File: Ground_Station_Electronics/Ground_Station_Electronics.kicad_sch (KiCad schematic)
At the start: 4 parts

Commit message: worked on rs485
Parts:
- removed J?: (no value), symbol Connector:RJ45_Shielded
- removed R?: R_Small, symbol Device:R_Small
- added C? (x2): 33u, symbol Device:C_Polarized_Small
- added C?: (no value), symbol Device:C_Small
- added C?: (no value), symbol Device:C_Polarized_Small
- added J?: (no value), symbol GS_Library:RJ45_Shielded_Labelled
- added R?: 120, Resistor_SMD:R_0603_1608Metric, symbol Device:R_Small
- U?: value (none) -> MAX3488E; footprint (none) -> Package_SO:SOIC-8_3.9x4.9mm_P1.27mm
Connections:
- net at R?.1: now also U?.5 (Y), J?.6 (ORG)
- net at R?.2: now also U?.6 (Z), J?.3 (~{ORG})
- net +3V3: now reaches U?.1 (VCC)
- net +3V3: now also C?.2
- net GND: now reaches U?.4 (GND)
- net GND: now also C?.1, C?.2, C?.2, C?.2, J?.7 (~{BRN}), J?.8 (BRN), J?.SH
- net at U?.7 (B): now also J?.1 (~{GRN}), R?.2
- net at U?.8 (A): now also J?.2 (GRN), R?.1
- new net +12V: C?.1, C?.1, C?.1, J?.4 (BLU), J?.5 (~{BLU})
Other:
- moved on the sheet: R?, U?

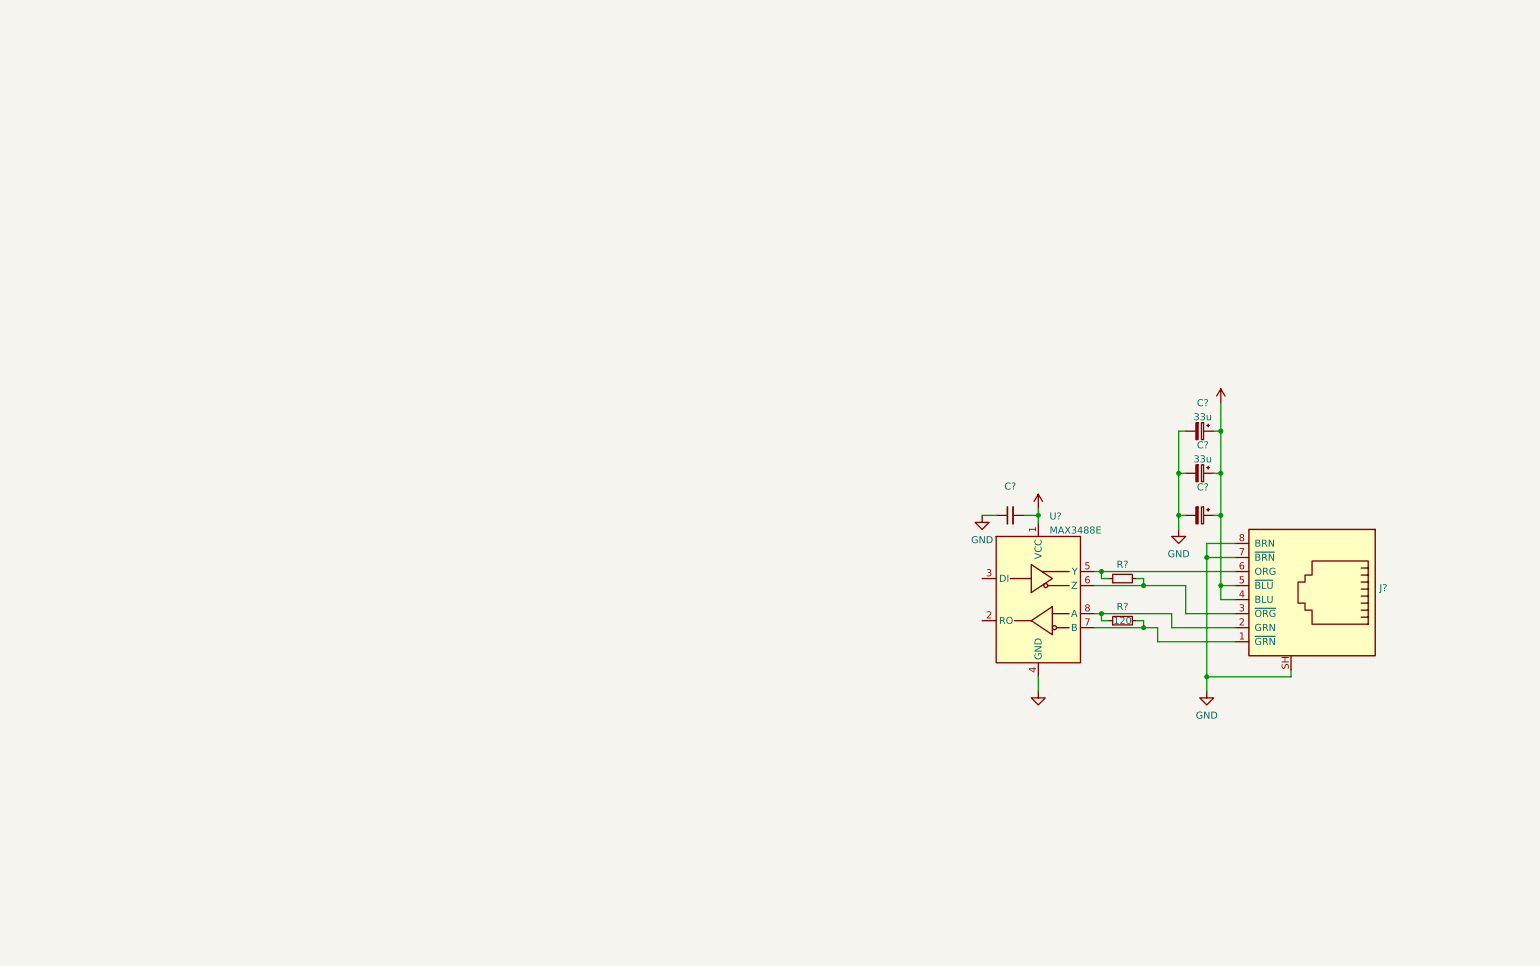
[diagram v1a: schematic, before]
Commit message: Take 2 Electric Boogaloo
Migrated to KiCad 6.0. Re-added the schematic stuff from last time in the new version, hopefully with working libraries
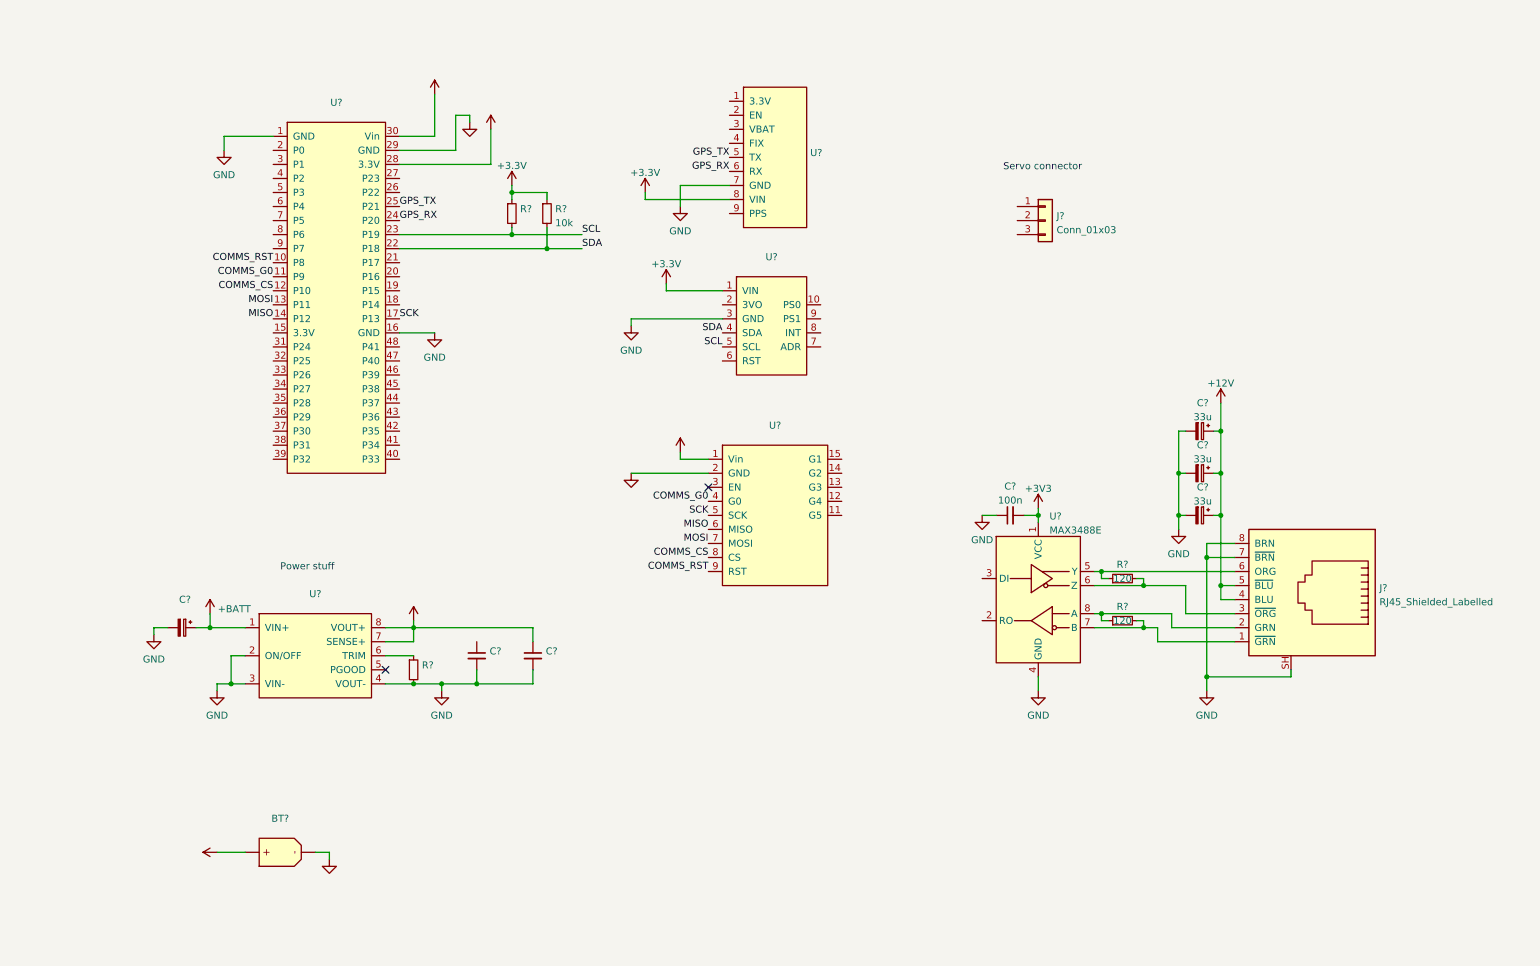
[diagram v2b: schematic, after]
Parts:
- added BT?: (no value), symbol ASTRA_Library:XT60_Battery_Connector
- added C? (x2): (no value), symbol Device:C_Small
- added C?: (no value), symbol Device:C_Polarized_Small
- added J?: Conn_01x03, symbol Connector_Generic:Conn_01x03
- added R?: 10k, symbol Device:R_Small
- added R? (x2): (no value), symbol Device:R_Small
- added U?: (no value), symbol MainElectronicsLib:BNO055_Adafruit_Breakout
- added U?: (no value), symbol ASTRA_Library:Teensy_4.1
- added U?: (no value), symbol ASTRA_Library:Adafruit_GPS_V3
- added U?: (no value), symbol MainElectronicsLib:RFM95W_Adafruit_Breakout
- added U?: (no value), symbol ASTRA_Library:TDK_I3A4W008A033V
- C?: value (none) -> 100n; footprint (none) -> Capacitor_SMD:C_0603_1608Metric
- C?: value (none) -> 33u
- J?: value (none) -> RJ45_Shielded_Labelled
- R?: value (none) -> 120; footprint (none) -> Resistor_SMD:R_0603_1608Metric
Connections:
- net +3V3: now also R?.1, R?.1, U?.1 (VIN), U?.1 (Vin), U?.28 (3.3V), U?.8 (VIN)
- net GND: now also BT?.1 (Neg), C?.2, C?.2, C?.2, R?.2, U?.1 (GND), U?.16 (GND), U?.2 (GND), U?.2 (ON/OFF), U?.29 (GND), U?.3 (GND), U?.3 (VIN-), U?.4 (VOUT-), U?.7 (GND)
- new net: R?.1, U?.6 (TRIM)
- new net +5V: C?.1, U?.30 (Vin), U?.7 (SENSE+), U?.8 (VOUT+)
- new net +BATT: BT?.2 (Pos), C?.1, U?.1 (VIN+)
- new net COMMS_CS: U?.12 (P10), U?.8 (CS)
- new net COMMS_G0: U?.11 (P9), U?.4 (G0)
- new net COMMS_RST: U?.10 (P8), U?.9 (RST)
- new net GPS_RX: U?.24 (P20), U?.6 (RX)
- new net GPS_TX: U?.25 (P21), U?.5 (TX)
- new net MISO: U?.14 (P12), U?.6 (MISO)
- new net MOSI: U?.13 (P11), U?.7 (MOSI)
- new net SCK: U?.17 (P13), U?.5 (SCK)
- new net SCL: R?.2, U?.23 (P19), U?.5 (SCL)
- new net SDA: R?.2, U?.22 (P18), U?.4 (SDA)
- no-connect marks 0 -> 2
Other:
- note added: "Power stuff"
- note added: "Servo connector"

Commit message: Working on schematic
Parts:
- removed C? (x2): (no value), symbol Device:C_Small
- removed C?: (no value), symbol Device:C_Polarized_Small
- removed J?: Conn_01x03, symbol Connector_Generic:Conn_01x03
- removed R?: (no value), symbol Device:R_Small
- removed U?: (no value), symbol ASTRA_Library:TDK_I3A4W008A033V
- added C1, C2: (no value), symbol Device:C_Polarized_Small_US
- added C3: 100u, symbol Device:C_Polarized_Small_US
- added C8: 1m, symbol Device:C_Polarized_Small_US
- added C9: 100n, Capacitor_SMD:C_0603_1608Metric, symbol Device:C_Small
- added D1: (no value), symbol Device:D_Schottky
- added D2: (no value), symbol Device:LED_Small
- added D3, D4: G, LED_SMD:LED_0603_1608Metric_Pad1.05x0.95mm_HandSolder, symbol Device:LED_Small
- added J2: (no value), symbol Connector_Generic:Conn_01x03
- added L1: (no value), symbol Device:L
- added M1: (no value), symbol GS_Library:Motor_Servo
- added M2: Motor_Servo, symbol GS_Library:Motor_Servo
- added R1, R2, R4: (no value), symbol Device:R_Small
- added U1: (no value), symbol Regulator_Switching:LM2576HVS-5
- added U7: (no value), symbol ASTRA_Library:SN74AHCT125D
- C5, C6: renamed from C?; symbol Device:C_Polarized_Small -> Device:C_Polarized_Small_US
- C7: renamed from C?; value 33u -> (none); symbol Device:C_Polarized_Small -> Device:C_Polarized_Small_US
- R3: renamed from R?; value (none) -> 10k
- U2: renamed from U?; value (none) -> Teensy_4.1
- U3: renamed from U?; value (none) -> Adafruit_GPS_V3
- U4: renamed from U?; value (none) -> BNO055_Adafruit_Breakout
- U5: renamed from U?; value (none) -> RFM95W_Adafruit_Breakout
- gave numbers to parts that had none: 7
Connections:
- net +BATT is gone; now on net +24V: BT1.2 (Pos)
- net +3V3: now also D2.2 (A)
- net +5V: now also C2.1, C3.1, C8.1, C9.2, D3.2 (A), J2.1 (Pin_1), L1.2, M1.2 (+), M2.2 (+), U1.4 (FB), U7.14 (VCC)
- net GND: now also C1.2, C2.2, C3.2, C8.2, C9.1, D1.2 (A), J2.2 (Pin_2), M1.3 (-), M2.3 (-), R1.2, R2.2, R4.2, U1.3 (GND), U1.5 (~{ON}/OFF), U7.1 (1~{OE}), U7.10 (3~{OE}), U7.11 (4Y), U7.12 (4A), U7.13 (4~{OE}), U7.4 (2~{OE}), U7.5 (2A), U7.6 (2Y), U7.7 (GND), U7.8 (3Y), U7.9 (3A)
- net COMP_RX: now reaches U6.2 (RO)
- net COMP_RX: now also U2.3 (P1)
- net COMP_TX: now reaches U6.3 (DI)
- net COMP_TX: now also U2.2 (P0)
- net SRV1_PWM: now reaches U2.4 (P2)
- net SRV1_PWM: now also M1.1 (PWM)
- net SRV2_PWM: now reaches U2.5 (P3)
- net SRV2_PWM: now also M2.1 (PWM)
- net +12V renamed +24V
- net +24V: now also C1.1, D4.2 (A), U1.1 (VIN)
- new net: D3.1 (K), R2.1
- new net: J2.3 (Pin_3), U7.3 (1Y)
- new net: D4.1 (K), R4.1
- new net: D1.1 (K), L1.1, U1.2 (OUT)
- new net: D2.1 (K), R1.1
- no-connect marks 2 -> 1
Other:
- note removed: "Servo connector"

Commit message: worked on schematic and footprints
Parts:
- C1: Digikey Part Num (none) -> 50PEV100M10X10.5CT-ND
- C2: Digikey Part Num (none) -> P16300-ND
- C3: value 100u -> (none); Digikey Part Num (none) -> 50PEV100M10X10.5CT-ND
- C4, C9: value 100n -> (none); footprint Capacitor_SMD:C_0603_1608Metric -> (none)
- C5, C6: value 33u -> (none); Digikey Part Num (none) -> 493-4402-1-ND
- C7: Digikey Part Num (none) -> 493-4402-1-ND
- C8: value 1m -> (none); Digikey Part Num (none) -> P16300-ND
- D1: Digikey Part Num (none) -> B560C-FDICT-ND
- D3, D4: value G -> (none); footprint LED_SMD:LED_0603_1608Metric_Pad1.05x0.95mm_HandSolder -> (none)
- J1: value RJ45_Shielded_Labelled -> (none); Digikey Part Num (none) -> AE10387-ND
- L1: Digikey Part Num (none) -> 732-11715-ND
- M2: value Motor_Servo -> (none)
- R1: Digikey Part Num (none) -> 311-10.0HRCT-ND
- R2: Digikey Part Num (none) -> 311-180HRCT-ND
- R3, R5: value 10k -> (none)
- R4: Digikey Part Num (none) -> 311-3.30KHRCT-ND
- R6, R7: value 120 -> (none); footprint Resistor_SMD:R_0603_1608Metric -> (none); Digikey Part Num (none) -> RMCF0603FT120RCT-ND
- U1: Digikey Part Num (none) -> LM2576HVS-5.0/NOPB-ND
- U2: value Teensy_4.1 -> (none); Digikey Part Num (none) -> 1568-DEV-16996-ND
- U3: value Adafruit_GPS_V3 -> (none); Digikey Part Num (none) -> 1528-1153-ND
- U4: value BNO055_Adafruit_Breakout -> (none); Digikey Part Num (none) -> 1528-4646-ND
- U5: value RFM95W_Adafruit_Breakout -> (none); Digikey Part Num (none) -> 1528-1667-ND
- U6: value MAX3488E -> (none); footprint Package_SO:SOIC-8_3.9x4.9mm_P1.27mm -> (none); Digikey Part Num (none) -> MAX3488EESA+TCT-ND
- U7: Digikey Part Num (none) -> 296-4652-5-ND

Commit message: should be schematic done?
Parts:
- added D?: (no value), symbol Device:D_Zener
- added F?: (no value), symbol Device:Polyfuse
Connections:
- net +24V: now also F?.2; no longer C1.1, U1.1 (VIN)
- net GND: now also D?.2 (A)
- new net: C1.1, D?.1 (K), F?.1, U1.1 (VIN)
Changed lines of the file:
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@@
   (junction (at 246.38 45.72) (diameter 0) (color 0 0 0 0)
   )
+  (junction (at 31.75 132.08) (diameter 0) (color 0 0 0 0)
+  )
   (junction (at 113.03 60.96) (diameter 0) (color 0 0 0 0)
   )
@@
   )
   (junction (at 91.44 137.16) (diameter 0) (color 0 0 0 0)
+  )
+  (junction (at 43.18 146.05) (diameter 0) (color 0 0 0 0)
   )
   (junction (at 106.68 58.42) (diameter 0) (color 0 0 0 0)
@@
     (stroke (width 0) (type default) (color 0 0 0 0))
   )
+  (wire (pts (xy 31.75 146.05) (xy 31.75 142.24))
+    (stroke (width 0) (type default) (color 0 0 0 0))
+  )
   (wire (pts (xy 102.87 45.72) (xy 102.87 39.37))
     (stroke (width 0) (type default) (color 0 0 0 0))
@@
     (stroke (width 0) (type default) (color 0 0 0 0))
   )
-  (wire (pts (xy 40.64 132.08) (xy 43.18 132.08))
+  (wire (pts (xy 29.21 132.08) (xy 31.75 132.08))
     (stroke (width 0) (type default) (color 0 0 0 0))
   )
@@
     (stroke (width 0) (type default) (color 0 0 0 0))
   )
+  (wire (pts (xy 43.18 146.05) (xy 31.75 146.05))
+    (stroke (width 0) (type default) (color 0 0 0 0))
+  )
   (wire (pts (xy 107.95 129.54) (xy 93.98 129.54))
     (stroke (width 0) (type default) (color 0 0 0 0))
@@
     (stroke (width 0) (type default) (color 0 0 0 0))
   )
+  (wire (pts (xy 19.05 132.08) (xy 21.59 132.08))
+    (stroke (width 0) (type default) (color 0 0 0 0))
+  )
   (wire (pts (xy 212.09 129.54) (xy 220.98 129.54))
     (stroke (width 0) (type default) (color 0 0 0 0))
@@
     (stroke (width 0) (type default) (color 0 0 0 0))
   )
+  (wire (pts (xy 31.75 132.08) (xy 43.18 132.08))
+    (stroke (width 0) (type default) (color 0 0 0 0))
+  )
   (wire (pts (xy 191.77 109.22) (xy 194.31 109.22))
     (stroke (width 0) (type default) (color 0 0 0 0))
@@
   )
   (wire (pts (xy 137.16 53.34) (xy 137.16 49.53))
+    (stroke (width 0) (type default) (color 0 0 0 0))
+  )
+  (wire (pts (xy 31.75 132.08) (xy 31.75 134.62))
     (stroke (width 0) (type default) (color 0 0 0 0))
   )
@@
     )
     (pin "1")
+  )
+  (symbol (lib_id "Device:D_Zener") (at 31.75 138.43 270) (unit 1)
+    (in_bom yes) (on_board yes) (fields_autoplaced)
+    (property "Reference" "D?" (id 0) (at 33.782 137.5953 90)
+      (effects (font (size 1.27 1.27)) (justify left))
+    )
+    (property "Value" "" (id 1) (at 33.782 140.1322 90)
+      (effects (font (size 1.27 1.27)) (justify left))
+    )
+    (property "Footprint" "" (id 2) (at 31.75 138.43 0)
+      (effects (font (size 1.27 1.27)) hide)
+    )
+    (property "Datasheet" "~" (id 3) (at 31.75 138.43 0)
+      (effects (font (size 1.27 1.27)) hide)
+    )
+    (property "Digikey Part Num" "1655-SMBJ36ACT-ND" (id 4) (at 31.75 138.43 0)
+      (effects (font (size 1.27 1.27)) hide)
+    )
+    (pin "1")
+    (pin "2")
   )
   (symbol (lib_id "power:GND") (at 181.61 49.53 0) (unit 1)
@@
     (pin "1")
   )
-  (symbol (lib_id "power:+24V") (at 40.64 132.08 0) (unit 1)
-    (in_bom yes) (on_board yes) (fields_autoplaced)
-    (property "Reference" "#PWR03" (id 0) (at 40.64 135.89 0)
-      (effects (font (size 1.27 1.27)) hide)
-    )
-    (property "Value" "+24V" (id 1) (at 40.64 128.5042 0))
-    (property "Footprint" "" (id 2) (at 40.64 132.08 0)
-      (effects (font (size 1.27 1.27)) hide)
-    )
-    (property "Datasheet" "" (id 3) (at 40.64 132.08 0)
+  (symbol (lib_id "power:+24V") (at 19.05 132.08 0) (unit 1)
+    (in_bom yes) (on_board yes)
+    (property "Reference" "#PWR03" (id 0) (at 19.05 135.89 0)
+      (effects (font (size 1.27 1.27)) hide)
+    )
+    (property "Value" "+24V" (id 1) (at 19.05 128.5042 0))
+    (property "Footprint" "" (id 2) (at 19.05 132.08 0)
+      (effects (font (size 1.27 1.27)) hide)
+    )
+    (property "Datasheet" "" (id 3) (at 19.05 132.08 0)
       (effects (font (size 1.27 1.27)) hide)
     )
@@
     (pin "1")
   )
+  (symbol (lib_id "Device:Polyfuse") (at 25.4 132.08 270) (unit 1)
+    (in_bom yes) (on_board yes) (fields_autoplaced)
+    (property "Reference" "F?" (id 0) (at 25.4 126.9832 90))
+    (property "Value" "" (id 1) (at 25.4 129.5201 90))
+    (property "Footprint" "" (id 2) (at 20.32 133.35 0)
+      (effects (font (size 1.27 1.27)) (justify left) hide)
+    )
+    (property "Datasheet" "~" (id 3) (at 25.4 132.08 0)
+      (effects (font (size 1.27 1.27)) hide)
+    )
+    (property "Digikey Part Num" "507-1747-1-ND" (id 4) (at 25.4 132.08 0)
+      (effects (font (size 1.27 1.27)) hide)
+    )
+    (pin "1")
+    (pin "2")
+  )
   (symbol (lib_id "power:+3.3V") (at 95.25 167.64 0) (unit 1)
     (in_bom yes) (on_board yes) (fields_autoplaced)
@@
       (reference "D4") (unit 1) (value "G") (footprint "LED_SMD:LED_0603_1608Metric_Pad1.05x0.95mm_HandSolder")
     )
+    (path "/089dbcda-11ac-4d31-a495-440161ba5d49"
+      (reference "D?") (unit 1) (value "D_Zener") (footprint "Diode_SMD:D_SMB_Handsoldering")
+    )
+    (path "/b963ab2b-e2a6-43d1-86d1-7b2176c8f88b"
+      (reference "F?") (unit 1) (value "Polyfuse") (footprint "Fuse:Fuse_2920_7451Metric_Pad2.10x5.45mm_HandSolder")
+    )
     (path "/9d8a2d54-0360-4e43-a3a9-429b299a601f"
       (reference "J1") (unit 1) (value "RJ45_Shielded_Labelled") (footprint "Connector_RJ:RJ45_Amphenol_RJHSE5380")
@@
     )
     (path "/35ea9ade-8a46-40ba-b7b7-ecea6ac62ecf"
-      (reference "U2") (unit 1) (value "Teensy_4.1") (footprint "")
+      (reference "U2") (unit 1) (value "Teensy_4.1") (footprint "ASTRA_Footprints:Teensy4.1")
     )
     (path "/87b13742-a5cd-4d8c-9371-c8fc551cffdc"
-      (reference "U3") (unit 1) (value "Adafruit_GPS_V3") (footprint "")
+      (reference "U3") (unit 1) (value "Adafruit_GPS_V3") (footprint "ASTRA_Footprints:Adafruit_GPS_Breakout")
     )
     (path "/1a3e270c-4303-465c-8ec0-d330d0f7d465"
-      (reference "U4") (unit 1) (value "BNO055_Adafruit_Breakout") (footprint "")
+      (reference "U4") (unit 1) (value "BNO055_Adafruit_Breakout") (footprint "GS_Library:Adafruit_BNO055")
     )
     (path "/9908e0ef-a0e9-4118-a3e2-9d9b094c25f3"
-      (reference "U5") (unit 1) (value "RFM95W_Adafruit_Breakout") (footprint "")
+      (reference "U5") (unit 1) (value "RFM95W_Adafruit_Breakout") (footprint "ASTRA_Footprints:Adafruit_RFM95W")
     )
     (path "/290d2dfd-ee9c-4622-bfa5-cc5385e151ab"

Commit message: Forgot to save schematic
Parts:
- gave numbers to parts that had none: 2
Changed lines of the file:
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@@
   (symbol (lib_id "Device:D_Zener") (at 31.75 138.43 270) (unit 1)
     (in_bom yes) (on_board yes) (fields_autoplaced)
-    (property "Reference" "D?" (id 0) (at 33.782 137.5953 90)
+    (property "Reference" "D5" (id 0) (at 33.782 137.5953 90)
       (effects (font (size 1.27 1.27)) (justify left))
     )
@@
   (symbol (lib_id "Device:Polyfuse") (at 25.4 132.08 270) (unit 1)
     (in_bom yes) (on_board yes) (fields_autoplaced)
-    (property "Reference" "F?" (id 0) (at 25.4 126.9832 90))
+    (property "Reference" "F1" (id 0) (at 25.4 126.9832 90))
     (property "Value" "" (id 1) (at 25.4 129.5201 90))
     (property "Footprint" "" (id 2) (at 20.32 133.35 0)
@@
     )
     (path "/089dbcda-11ac-4d31-a495-440161ba5d49"
-      (reference "D?") (unit 1) (value "D_Zener") (footprint "Diode_SMD:D_SMB_Handsoldering")
+      (reference "D5") (unit 1) (value "D_Zener") (footprint "Diode_SMD:D_SMB_Handsoldering")
     )
     (path "/b963ab2b-e2a6-43d1-86d1-7b2176c8f88b"
-      (reference "F?") (unit 1) (value "Polyfuse") (footprint "Fuse:Fuse_2920_7451Metric_Pad2.10x5.45mm_HandSolder")
+      (reference "F1") (unit 1) (value "Polyfuse") (footprint "Fuse:Fuse_2920_7451Metric_Pad2.10x5.45mm_HandSolder")
     )
     (path "/9d8a2d54-0360-4e43-a3a9-429b299a601f"

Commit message: design rules and grouping
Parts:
- removed C6, C7: (no value), symbol Device:C_Polarized_Small_US
- C5: value (none) -> 100u; footprint (none) -> Capacitor_SMD:CP_Elec_10x10; Digikey Part Num 493-4402-1-ND -> 50PEV100M10X10.5CT-ND

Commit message: Layout and routing
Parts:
- removed C5: 100u, Capacitor_SMD:CP_Elec_10x10, symbol Device:C_Polarized_Small_US
- J1: Digikey Part Num AE10387-ND -> RJHSE5E80-ND
- renumbered C8 to C5, C9 to C6, D2 to D1, D3 to D2, D4 to D3, D5 to D4, D1 to D5, R4 to R3, R3 to R4
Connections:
- net +24V: now also J1.6 (ORG); no longer J1.4 (BLU)
- net GND: now also J1.3 (~{ORG}), J1.4 (BLU); no longer J1.7 (~{BRN}), J1.8 (BRN)
- net TX_P: now reaches R6.1, U6.5 (Y)
- net TX_P: now also J1.7 (~{BRN}); no longer J1.6 (ORG)
- net TX_N: now reaches R6.2, U6.6 (Z)
- net TX_N: now also J1.8 (BRN); no longer J1.3 (~{ORG})
- net RX_N: now reaches R7.2, U6.7 (B)
- net RX_N: now also J1.2 (GRN); no longer J1.1 (~{GRN})
- net RX_P: now reaches R7.1, U6.8 (A)
- net RX_P: now also J1.1 (~{GRN}); no longer J1.2 (GRN)
- net ARGB_DATA: now reaches U2.6 (P4)
- net ARGB_DATA: now also U7.2 (1A)
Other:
- moved on the sheet: D1, D2, D3, R1, R2, R3
